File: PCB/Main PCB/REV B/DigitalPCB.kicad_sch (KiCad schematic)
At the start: 163 parts, among them J1 393570002, J10 Spare2, J2 Conn_01x03_Female, J3 1050170001, J4 Hopper, J5 393570002, J6 393570002, J7 Screen, J8 393570002, J9 Spare1, Q1 2N7002, Q2 2N7002, Q3 MBT3904DW1, Q4 2N7002, U1 AMS1117-3.3, U10 ALDP105W, U11 TLP2362TPR_E, U12 ALDP105W, U13 STM811SW16F, U2 TS5A23159DGS, U3 ESP32-WROOM-32UE_16MB, U4 MAX31855KASA, U5 TPS2115APWR, U6 TLP2362TPR_E, U7 ALDP105W, U8 CP2102N-A02-GQFN24, U9 TLP2362TPR_E

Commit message: PCB - Changed to Analog and Digital Board to solve interface headaches
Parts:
- removed C1, C11, C6, C9: 0.1uF 50V X7R 0603, Capacitor_SMD:C_0603_1608Metric, symbol Device:C
- removed C10, C2: 10uF 16V X5R 0805, Capacitor_SMD:C_0805_2012Metric, symbol Device:C
- removed C12: 0.01uF 50V X7R 0603, Capacitor_SMD:C_0603_1608Metric, symbol Device:C
- removed D10, D12, D7: Schottky 30v 200mA, Customs Smoker:RB521S30T1G-M, symbol Diode:1N6857UR
- removed D11, D6, D9: B 3.2 20mA 0603, LED_SMD:LED_0603_1608Metric, symbol Device:LED
- removed H3, H4: MountingHole, MountingHole:MountingHole_3.2mm_M3_DIN965_Pad, symbol Mechanical:MountingHole
- removed J1, J5, J6, J8: 393570002, CONN_393570002_MOL, symbol 0393570002:393570002
- removed J2: Conn_01x03_Female, Connector_PinHeader_2.54mm:PinHeader_1x03_P2.54mm_Vertical, symbol Connector:Conn_01x03_Female
- removed JP1, JP2, JP5: SolderJumper_3_Open, Jumper:SolderJumper-3_P1.3mm_Open_RoundedPad1.0x1.5mm, symbol Jumper:SolderJumper_3_Open
- removed PS1: IRM-10-3.3, Converter_ACDC:Converter_ACDC_MeanWell_IRM-10-xx_THT, symbol Converter_ACDC:IRM-10-3.3
- removed PS2: IRM-05-5, Converter_ACDC:Converter_ACDC_MeanWell_IRM-05-xx_THT, symbol Converter_ACDC:IRM-05-5
- removed Q1, Q2, Q4: 2N7002, Package_TO_SOT_SMD:SOT-23, symbol Transistor_FET:2N7002
- removed R1, R13, R27, R35: 10K 1% 0603, Resistor_SMD:R_0603_1608Metric, symbol Device:R_US
- removed R12, R26, R34: 91Ohm 1% 0603, Resistor_SMD:R_0603_1608Metric, symbol Device:R_US
- removed R17, R28, R37: 0 Ohm 0603, Resistor_SMD:R_0603_1608Metric, symbol Device:R_US
- removed TC1: Thermocouple_Block, Customs Smoker:K-TypeAdapter, symbol Device:Thermocouple_Block
- removed TP1, TP17, TP2, TP24, TP3, TP30, TP4, TP5, TP6, TP7, TP8, TP9: TP, TestPoint:TestPoint_Pad_D1.0mm, symbol Connector:TestPoint
- removed U10, U12, U7: ALDP105W, Customs Smoker:PAN_ALD_PAN, symbol ALDP105W:ALDP105W
- removed U2: TS5A23159DGS, Package_SO:VSSOP-10_3x3mm_P0.5mm, symbol Analog_Switch:TS5A23159DGS
- removed U4: MAX31855KASA, Package_SO:SOIC-8_3.9x4.9mm_P1.27mm, symbol Sensor_Temperature:MAX31855KASA
- added J?: DF12NC-20DS-0.5V_51_, Customs Smoker:HRS_DF12NC-20DS-0.5V_51_, symbol DF12NCRCPT:DF12NC-20DS-0.5V_51_
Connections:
- net +3.3VA: now also J?.1, J?.3, J?.5, J?.7
- net +5V: now also J?.11, J?.13, J?.9
- net GND: now also J?.10, J?.12, J?.14, J?.2, J?.4, J?.6, J?.8
- net MUX_OUT_+: now also J?.19
- net MUX_OUT_-: now also J?.18
- net Opto_Auger: now also J?.15
- net Opto_Fan: now also J?.16
- net Opto_Ignitor: now also J?.17
- new net MuxSignal: J?.20
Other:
- note added: "INTERFACE"
- note removed: "AC-DC MAIN"
- note removed: "Mount probe jack on front plate"
- note removed: "Pull Low"
- note removed: "Thermocouples and Multiplexer"

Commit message: PCB - Rough Analog Layout
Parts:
- added H3, H4: MountingHole, MountingHole:MountingHole_3.2mm_M3_DIN965_Pad, symbol Mechanical:MountingHole
- gave numbers to parts that had none: 1
- renumbered C3 to C1, C17 to C10, C18 to C11, C19 to C12, C20 to C13, C21 to C14, C22 to C15, C23 to C16, C24 to C17, C25 to C18, C4 to C2, C5 to C3, C7 to C4, C8 to C5, C13 to C6, C14 to C7, C15 to C8, C16 to C9, D8 to D6, J3 to J2, J4 to J3, J7 to J4, J9 to J5, J10 to J6, JP3 to JP1, JP4 to JP2, JP6 to JP3, JP7 to JP4, JP8 to JP5, JP9 to JP6, Q3 to Q1, R2 to R1, R11 to R10, R14 to R11, R15 to R12, R16 to R13, R18 to R14, R19 to R15, R20 to R16, R21 to R17, R22 to R18, R23 to R19, R3 to R2, R24 to R20, R25 to R21, R29 to R22, R30 to R23, R31 to R24, R32 to R25, R33 to R26, R36 to R27, R38 to R28, R39 to R29, R4 to R3, R40 to R30, R41 to R31, R5 to R4, R6 to R5, R7 to R6, R8 to R7, R9 to R8, R10 to R9, TP10 to TP1, TP20 to TP10, TP21 to TP11, TP22 to TP12, TP23 to TP13, TP25 to TP14, TP26 to TP15, TP27 to TP16, TP28 to TP17, TP29 to TP18, TP31 to TP19, TP11 to TP2, TP32 to TP20, TP33 to TP21, TP34 to TP22, TP35 to TP23, TP36 to TP24, TP37 to TP25, TP38 to TP26, TP12 to TP3, TP13 to TP4, TP14 to TP5, TP15 to TP6, TP16 to TP7, TP18 to TP8, TP19 to TP9, U3 to U2, U5 to U3, U6 to U4, U8 to U5, U9 to U6, U11 to U7, U13 to U8

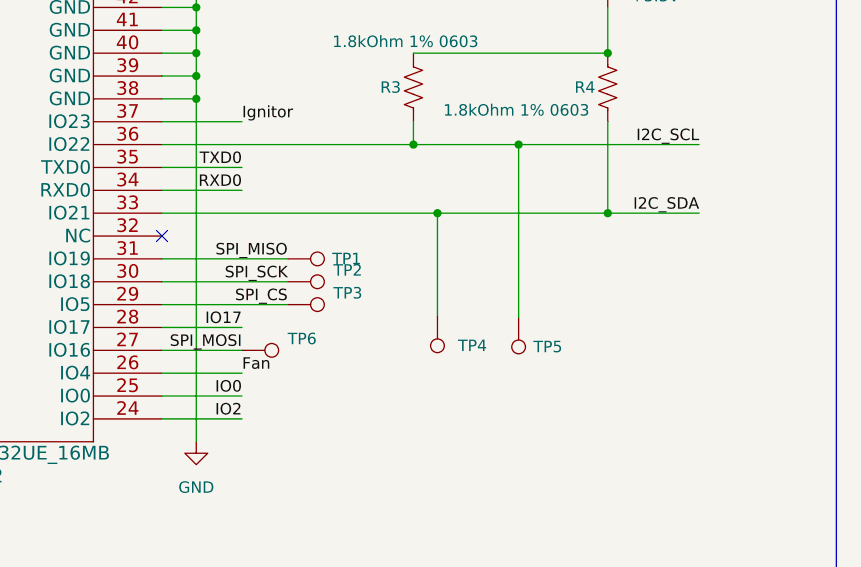
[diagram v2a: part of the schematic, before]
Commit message: PCB - Grouping for digital layout
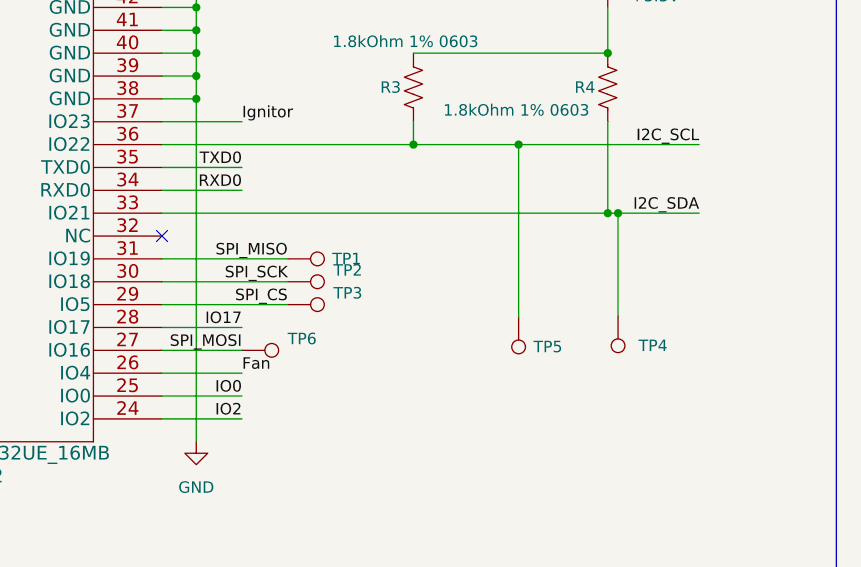
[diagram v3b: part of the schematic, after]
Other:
- moved on the sheet: TP4

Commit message: PCB - Digital/analog layout complete - ready to review
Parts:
- removed JP3, JP5: SolderJumper_3_Open, Jumper:SolderJumper-3_P1.3mm_Open_RoundedPad1.0x1.5mm, symbol Jumper:SolderJumper_3_Open
- removed R28, R30: 10K 1% 0603, Resistor_SMD:R_0603_1608Metric, symbol Device:R_US
- removed TP21, TP23: TP, TestPoint:TestPoint_Pad_D1.0mm, symbol Connector:TestPoint
- TP26: footprint Connector_PinHeader_2.54mm:PinHeader_1x06_P2.54mm_Vertical -> Connector_PinHeader_2.54mm:PinHeader_1x04_P2.54mm_Vertical; symbol Connector_Generic:Conn_01x06 -> Connector_Generic:Conn_01x04
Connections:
- net MUX_OUT_+ is gone; now on net MeatProbe+: J1.19
- net MUX_OUT_- is gone; now on net GND: J1.18
- net MuxSignal is gone; now on net MeatProbe-: J1.20
- net +5V: no longer J1.13
- net GND: no longer J1.14
- net IO13: now also TP26.4 (Pin_4); no longer TP26.6 (Pin_6)
- net IO12 renamed MeatProbe+
- net MeatProbe+: no longer TP26.5 (Pin_5)
- net IO14 renamed MeatProbe-
- net MeatProbe-: no longer TP26.4 (Pin_4)
- new net Probe1+: J1.13
- new net Probe1-: J1.14
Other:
- moved on the sheet: JP6, R31, TP24, TP7
